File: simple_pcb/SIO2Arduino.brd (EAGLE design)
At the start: 83.5 x 85.1 mm, 8 parts

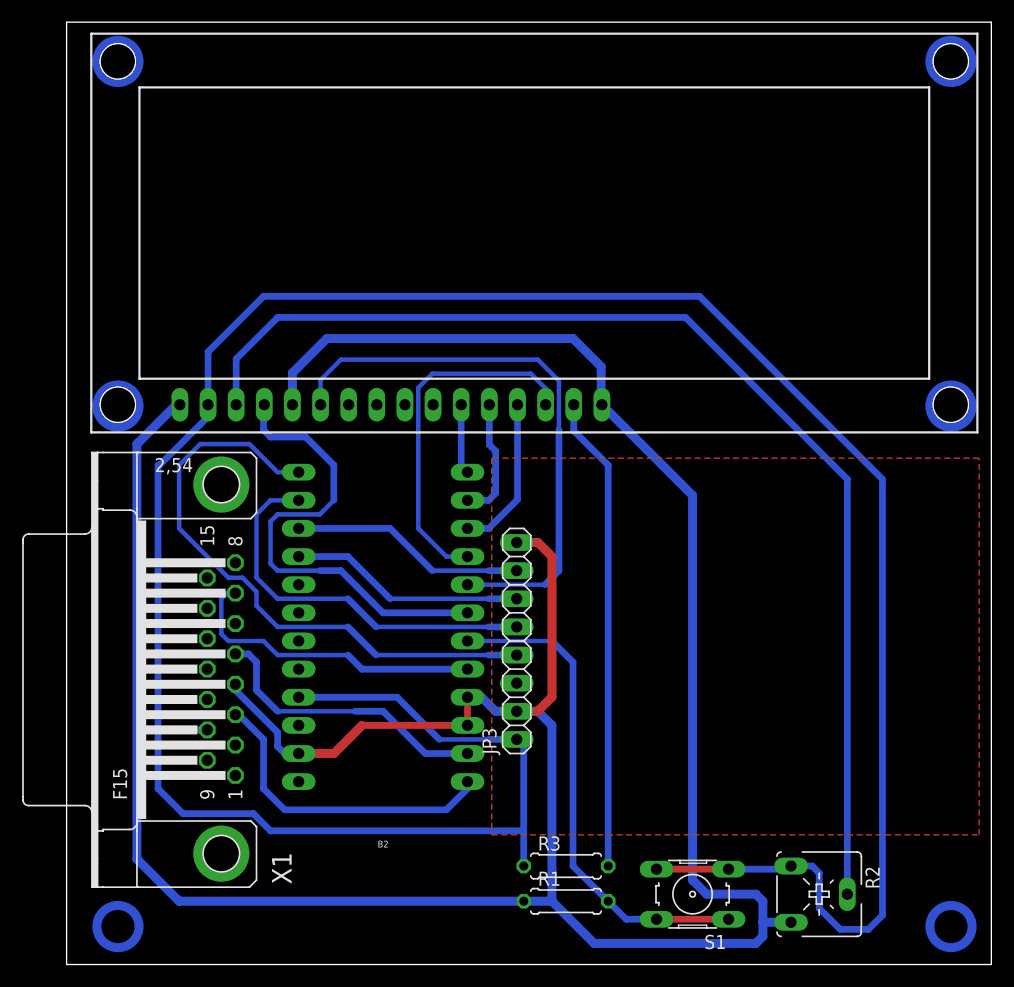
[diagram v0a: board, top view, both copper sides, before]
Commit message: Updated PCB with version number. Fixed readme
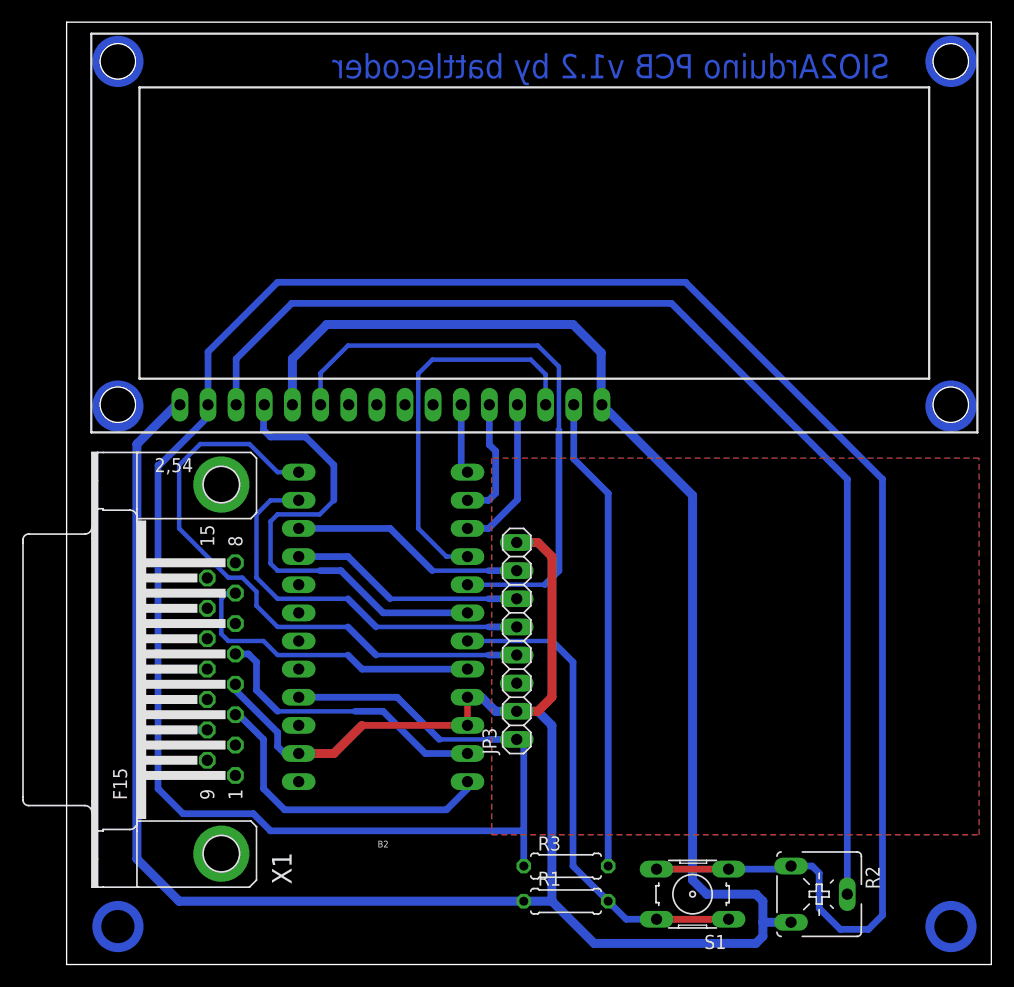
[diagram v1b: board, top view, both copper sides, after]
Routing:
- net LCD_D7: track 32.2 -> 34.8 mm
- net GND: track 271.3 -> 273.8 mm
- net LCD_EN: track 51.2 -> 53.4 mm
- net VCC: track 247.9 -> 249.0 mm
- net N$3: track 104.4 -> 105.4 mm
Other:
- board text added: "SIO2Arduino PCB v1.2 by battlecoder"
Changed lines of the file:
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@@
 <circle x="79.8449" y="51.054" radius="1.905" width="0.8128" layer="16"/>
 <circle x="79.8449" y="82.169" radius="1.905" width="0.8128" layer="16"/>
+<text x="74.295" y="80.645" size="2.1844" layer="16" ratio="5" rot="MR0">SIO2Arduino PCB v1.2 by battlecoder</text>
 </plain>
 <attributes>
@@
 <wire x1="19.05" y1="20.32" x2="19.685" y2="19.685" width="0.6096" layer="16"/>
 <wire x1="19.685" y1="19.685" x2="20.955" y2="19.685" width="0.6096" layer="16"/>
-<wire x1="20.3875" y1="51.175" x2="20.3875" y2="54.0425" width="0.8128" layer="16"/>
-<wire x1="20.3875" y1="54.0425" x2="23.495" y2="57.15" width="0.8128" layer="16"/>
-<wire x1="23.495" y1="57.15" x2="45.72" y2="57.15" width="0.8128" layer="16"/>
-<wire x1="45.72" y1="57.15" x2="48.26" y2="54.61" width="0.8128" layer="16"/>
+<wire x1="20.3875" y1="51.175" x2="20.3875" y2="55.3125" width="0.8128" layer="16"/>
+<wire x1="20.3875" y1="55.3125" x2="23.495" y2="58.42" width="0.8128" layer="16"/>
+<wire x1="23.495" y1="58.42" x2="45.72" y2="58.42" width="0.8128" layer="16"/>
+<wire x1="45.72" y1="58.42" x2="48.26" y2="55.88" width="0.8128" layer="16"/>
 <wire x1="43.815" y1="22.225" x2="42.545" y2="23.495" width="0.8128" layer="16"/>
 <wire x1="42.545" y1="23.495" x2="40.64" y2="23.495" width="0.8128" layer="16"/>
 <contactref element="R2" pad="E"/>
 <wire x1="48.3275" y1="51.175" x2="48.26" y2="51.2425" width="0.8128" layer="16"/>
-<wire x1="48.26" y1="51.2425" x2="48.26" y2="54.61" width="0.8128" layer="16"/>
+<wire x1="48.26" y1="51.2425" x2="48.26" y2="55.88" width="0.8128" layer="16"/>
 <wire x1="48.3275" y1="51.175" x2="56.515" y2="42.9875" width="0.8128" layer="16"/>
 <wire x1="56.515" y1="42.9875" x2="56.515" y2="8.255" width="0.8128" layer="16"/>
@@
 <wire x1="72.39" y1="3.81" x2="73.66" y2="5.08" width="0.6096" layer="16"/>
 <wire x1="73.66" y1="5.08" x2="73.66" y2="44.45" width="0.6096" layer="16"/>
-<wire x1="73.66" y1="44.45" x2="57.15" y2="60.96" width="0.6096" layer="16"/>
+<wire x1="73.66" y1="44.45" x2="55.88" y2="62.23" width="0.6096" layer="16"/>
 <wire x1="12.7675" y1="51.175" x2="12.7675" y2="55.9475" width="0.6096" layer="16"/>
-<wire x1="12.7675" y1="55.9475" x2="17.78" y2="60.96" width="0.6096" layer="16"/>
-<wire x1="57.15" y1="60.96" x2="17.78" y2="60.96" width="0.6096" layer="16"/>
+<wire x1="12.7675" y1="55.9475" x2="19.05" y2="62.23" width="0.6096" layer="16"/>
+<wire x1="55.88" y1="62.23" x2="19.05" y2="62.23" width="0.6096" layer="16"/>
 <wire x1="41.275" y1="9.525" x2="41.275" y2="12.7" width="0.6096" layer="16"/>
 <contactref element="B2" pad="21"/>
@@
 <contactref element="R2" pad="S"/>
 <contactref element="U$1" pad="3"/>
-<wire x1="19.05" y1="59.055" x2="55.88" y2="59.055" width="0.6096" layer="16"/>
-<wire x1="55.88" y1="59.055" x2="70.485" y2="44.45" width="0.6096" layer="16"/>
+<wire x1="20.32" y1="60.325" x2="54.61" y2="60.325" width="0.6096" layer="16"/>
+<wire x1="54.61" y1="60.325" x2="70.485" y2="44.45" width="0.6096" layer="16"/>
 <wire x1="70.485" y1="6.985" x2="70.485" y2="44.45" width="0.6096" layer="16"/>
-<wire x1="19.05" y1="59.055" x2="15.3075" y2="55.3125" width="0.6096" layer="16"/>
+<wire x1="20.32" y1="60.325" x2="15.3075" y2="55.3125" width="0.6096" layer="16"/>
 <wire x1="15.3075" y1="55.3125" x2="15.3075" y2="51.175" width="0.6096" layer="16"/>
 </signal>
@@
 <contactref element="B2" pad="8"/>
 <contactref element="U$1" pad="6"/>
-<wire x1="24.765" y1="55.245" x2="42.545" y2="55.245" width="0.4064" layer="16"/>
-<wire x1="42.545" y1="55.245" x2="44.45" y2="53.34" width="0.4064" layer="16"/>
+<wire x1="25.4" y1="56.515" x2="42.545" y2="56.515" width="0.4064" layer="16"/>
+<wire x1="42.545" y1="56.515" x2="44.45" y2="54.61" width="0.4064" layer="16"/>
 <wire x1="43.18" y1="34.925" x2="36.195" y2="34.925" width="0.4064" layer="16"/>
-<wire x1="24.765" y1="55.245" x2="22.9275" y2="53.4075" width="0.4064" layer="16"/>
-<wire x1="22.9275" y1="53.4075" x2="22.9275" y2="51.175" width="0.4064" layer="16"/>
-<wire x1="44.45" y1="53.34" x2="44.45" y2="48.895" width="0.4064" layer="16"/>
+<wire x1="25.4" y1="56.515" x2="22.9275" y2="54.0425" width="0.4064" layer="16"/>
+<wire x1="22.9275" y1="54.0425" x2="22.9275" y2="51.175" width="0.4064" layer="16"/>
+<wire x1="44.45" y1="54.61" x2="44.45" y2="48.895" width="0.4064" layer="16"/>
 <wire x1="44.45" y1="48.895" x2="44.45" y2="36.195" width="0.6096" layer="16"/>
 <wire x1="43.18" y1="34.925" x2="44.45" y2="36.195" width="0.6096" layer="16"/>
@@
 <wire x1="36.195" y1="37.465" x2="34.29" y2="37.465" width="0.4064" layer="16"/>
 <wire x1="34.29" y1="37.465" x2="31.75" y2="40.005" width="0.4064" layer="16"/>
-<wire x1="31.75" y1="40.005" x2="31.75" y2="52.705" width="0.4064" layer="16"/>
-<wire x1="33.02" y1="53.975" x2="41.91" y2="53.975" width="0.4064" layer="16"/>
-<wire x1="41.91" y1="53.975" x2="43.2475" y2="52.6375" width="0.4064" layer="16"/>
-<wire x1="43.2475" y1="52.6375" x2="43.2475" y2="51.175" width="0.4064" layer="16"/>
-<wire x1="33.02" y1="53.975" x2="31.75" y2="52.705" width="0.4064" layer="16"/>
+<wire x1="31.75" y1="40.005" x2="31.75" y2="53.975" width="0.4064" layer="16"/>
+<wire x1="33.02" y1="55.245" x2="41.91" y2="55.245" width="0.4064" layer="16"/>
+<wire x1="41.91" y1="55.245" x2="43.2475" y2="53.9075" width="0.4064" layer="16"/>
+<wire x1="43.2475" y1="53.9075" x2="43.2475" y2="51.175" width="0.4064" layer="16"/>
+<wire x1="33.02" y1="55.245" x2="31.75" y2="53.975" width="0.4064" layer="16"/>
 </signal>
 <signal name="SD_OUTLINE">
@@
 <contactref element="U$1" pad="15"/>
 <contactref element="R3" pad="2"/>
-<wire x1="48.895" y1="45.72" x2="48.895" y2="9.525" width="0.6096" layer="16"/>
-<wire x1="48.895" y1="45.72" x2="45.7875" y2="48.8275" width="0.6096" layer="16"/>
-<wire x1="45.7875" y1="48.8275" x2="45.7875" y2="51.175" width="0.6096" layer="16"/>
+<wire x1="48.895" y1="43.18" x2="48.895" y2="9.525" width="0.6096" layer="16"/>
+<wire x1="48.895" y1="43.18" x2="45.7875" y2="46.2875" width="0.6096" layer="16"/>
+<wire x1="45.7875" y1="46.2875" x2="45.7875" y2="51.175" width="0.6096" layer="16"/>
 </signal>
 </signals>
